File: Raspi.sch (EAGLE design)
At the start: 12 parts

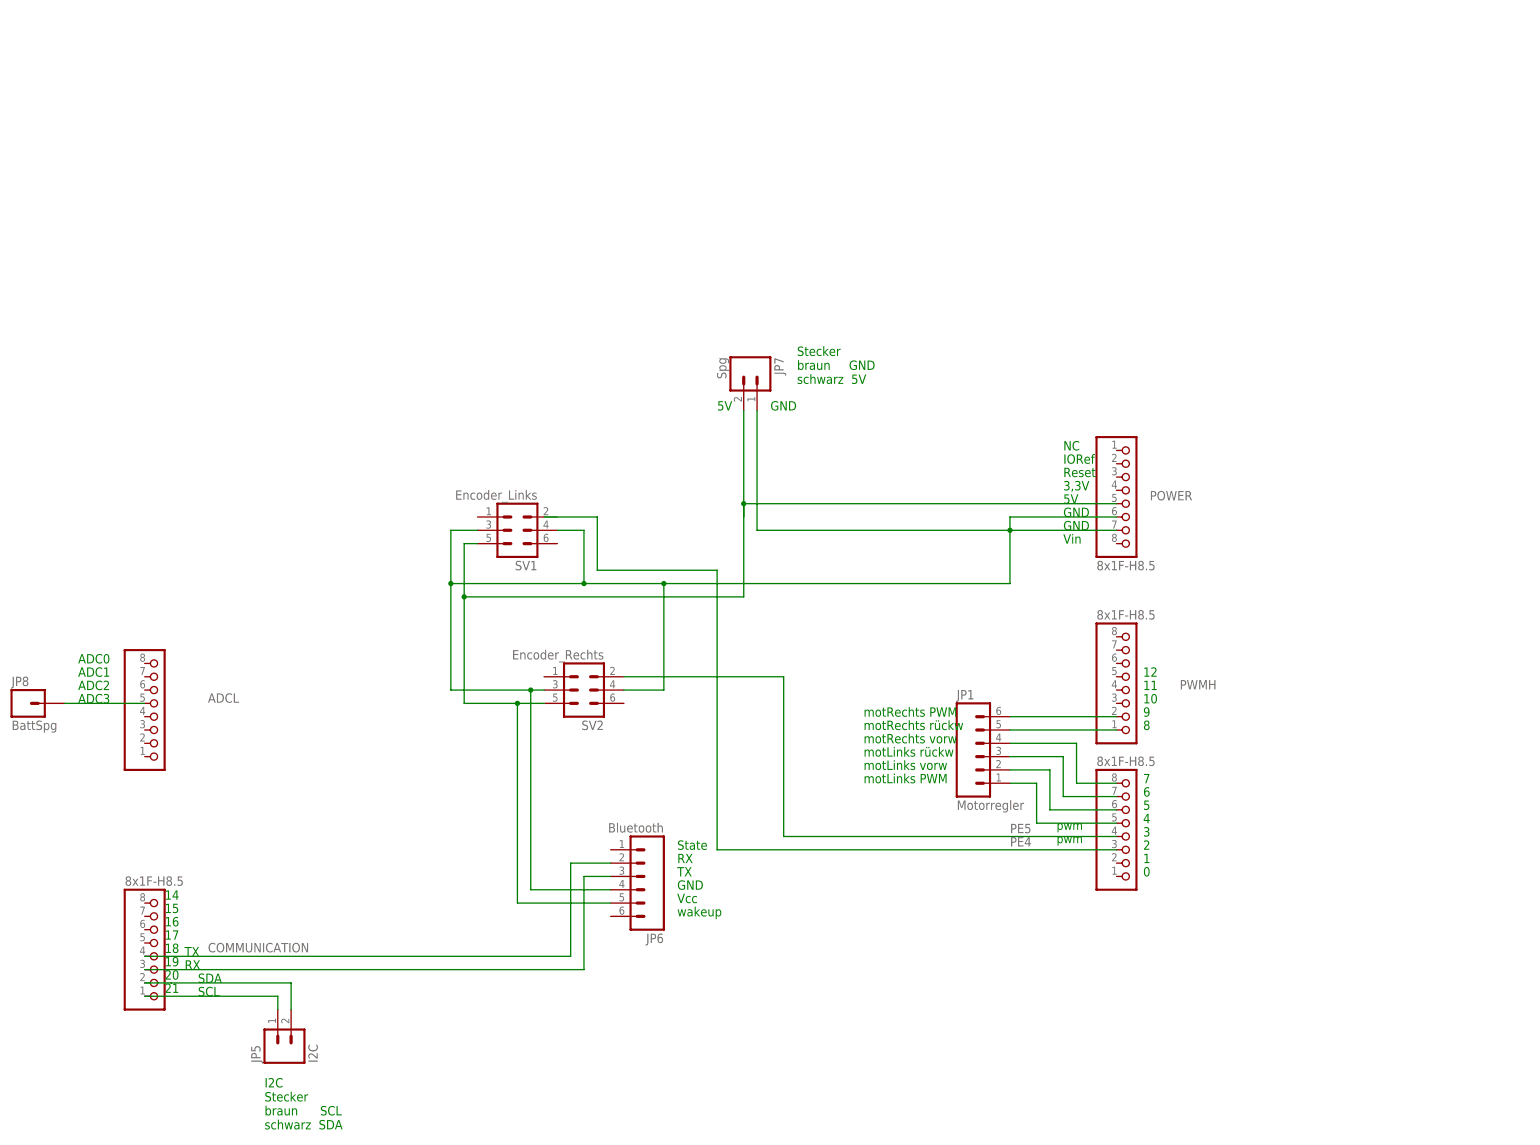
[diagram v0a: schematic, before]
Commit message: 
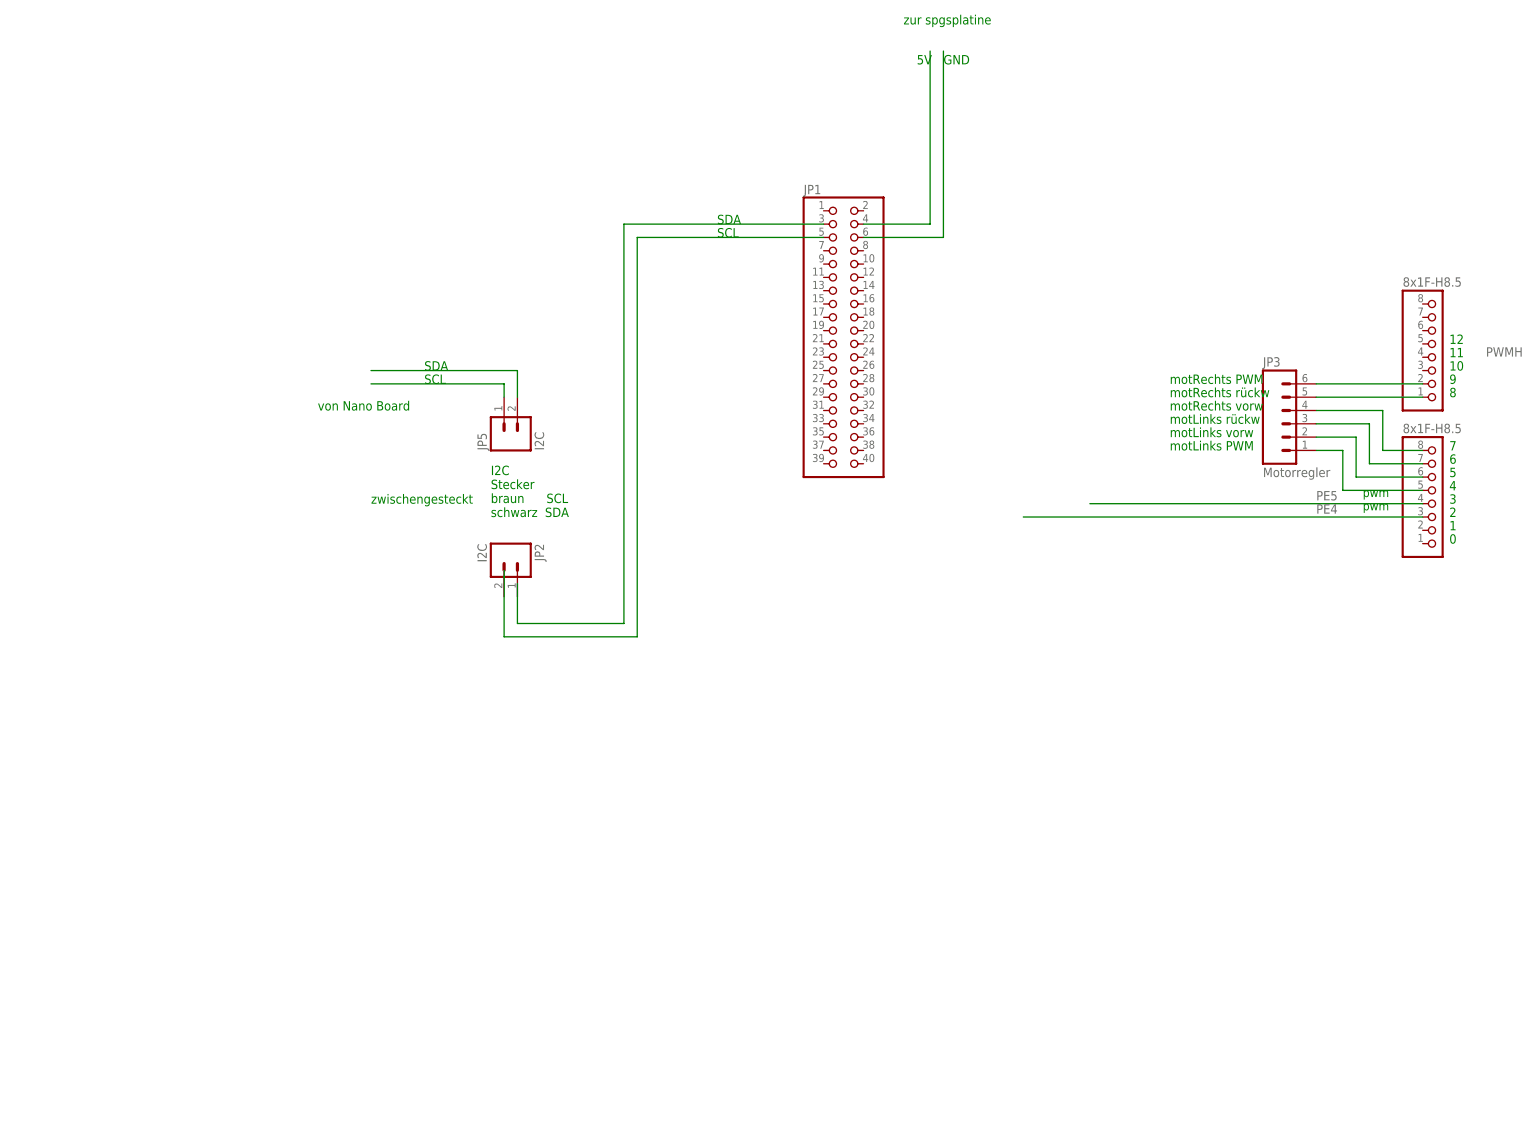
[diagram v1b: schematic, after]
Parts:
- removed ADCL, COMMUNICATION, POWER: 8x1F-H8.5, SmartPrj:PINHD-1X8
- removed JP6: Bluetooth, SparkFun-Connectors:M06LOCK
- removed JP7: Spg, SparkFun-Connectors:M02-JST-2MM-SMT
- removed JP8: BattSpg, SparkFun-Connectors:M01PTH
- removed SV1: Encoder_Links, con-ml:ML6
- removed SV2: Encoder_Rechts, con-ml:ML6
- added JP2: I2C, SparkFun-Connectors:M02-JST-2MM-SMT
- added JP3: Motorregler, SparkFun-Connectors:M06LOCK
- JP1: value Motorregler -> (none); device SparkFun-Connectors:M06LOCK -> adafruit:PINHD-2X20
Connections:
- removed net N$12: COMMUNICATION.3, JP6.3
- removed net N$13: COMMUNICATION.4, JP6.2
- new net N$6: JP3.5, PWMH.1
- net N$1: now also JP1.3; no longer JP6.5, JP7.1, POWER.5, SV1.5, SV2.5
- net N$10: no longer COMMUNICATION.1
- net N$11: no longer COMMUNICATION.2
- net N$16: now also JP3.4; no longer JP1.4
- net N$17: now also JP3.3; no longer JP1.3
- net N$18: now also JP3.2; no longer JP1.2
- net N$19: now also JP3.1; no longer JP1.1
- net N$2: now also JP1.5; no longer JP6.4, JP7.2, POWER.6, POWER.7, SV1.3, SV1.4, SV2.3, SV2.4
- net N$3: now also JP1.4; no longer JP1.6, PWMH.2
- net N$4: now also JP1.6; no longer JP1.5, PWMH.1
- net N$5: now also JP3.6, PWMH.2; no longer ADCL.5, JP8.1
- net PE5: no longer SV2.2
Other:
- note added: "von Nano Board"
- note added: "zur spgsplatine"
- note added: "zwischengesteckt"
- note removed: "14"
- note removed: "15"
- note removed: "16"
- note removed: "17"
- note removed: "18"
- note removed: "19"
- note removed: "20"
- note removed: "21"
- note removed: "3,3V"
- note removed: "ADC0"
- note removed: "ADC1"
- note removed: "ADC2"
- note removed: "ADC3"
- note removed: "IORef"
- note removed: "NC"
- note removed: "RX"
- note removed: "Reset"
- note removed: "State"
- note removed: "Stecker braun GND schwarz 5V"
- note removed: "TX"
- note removed: "Vcc"
- note removed: "Vin"
- note removed: "wakeup"
- moved on the sheet: JP5, PWMH

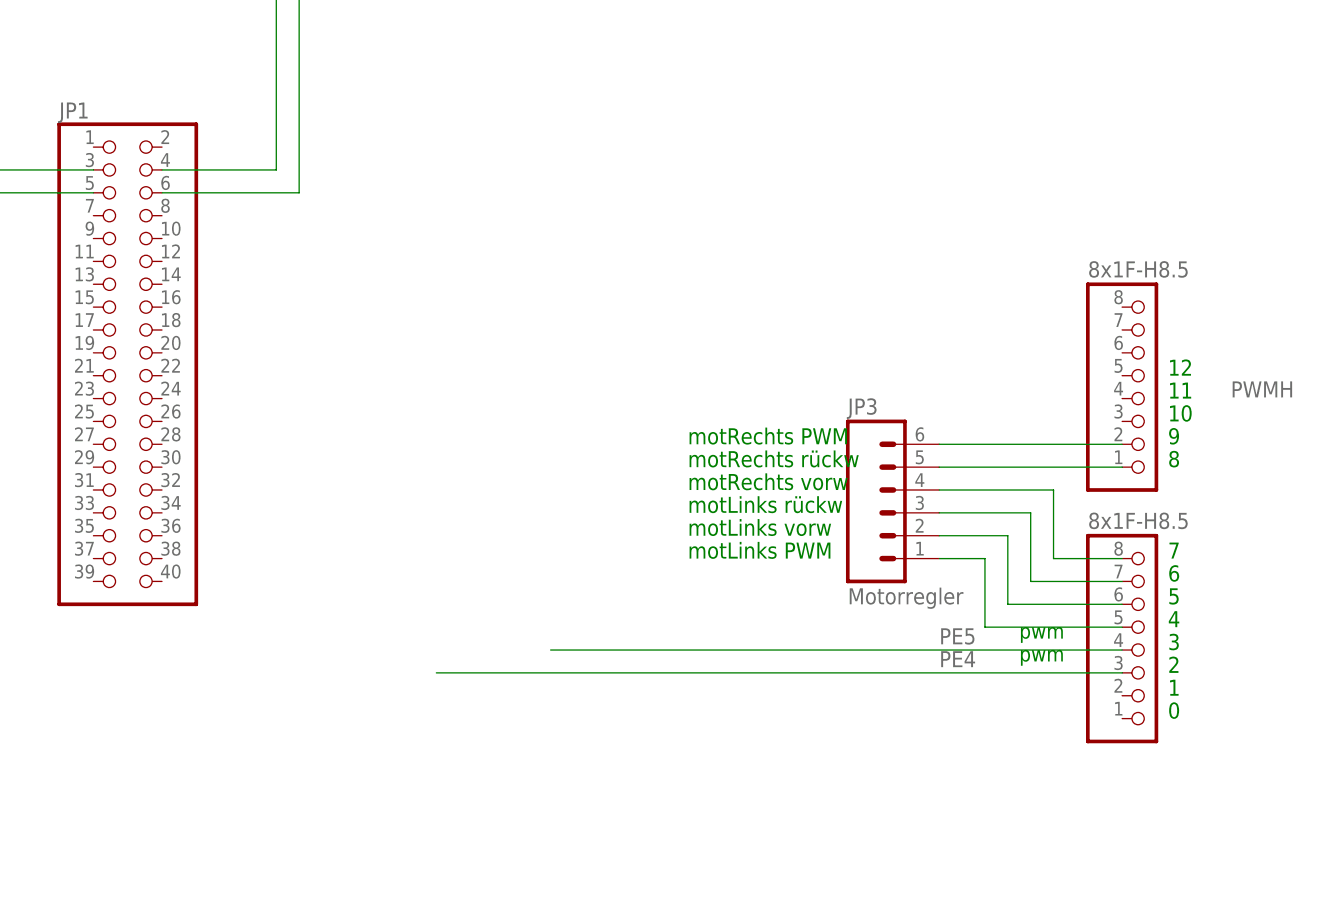
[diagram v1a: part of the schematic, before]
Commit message: 
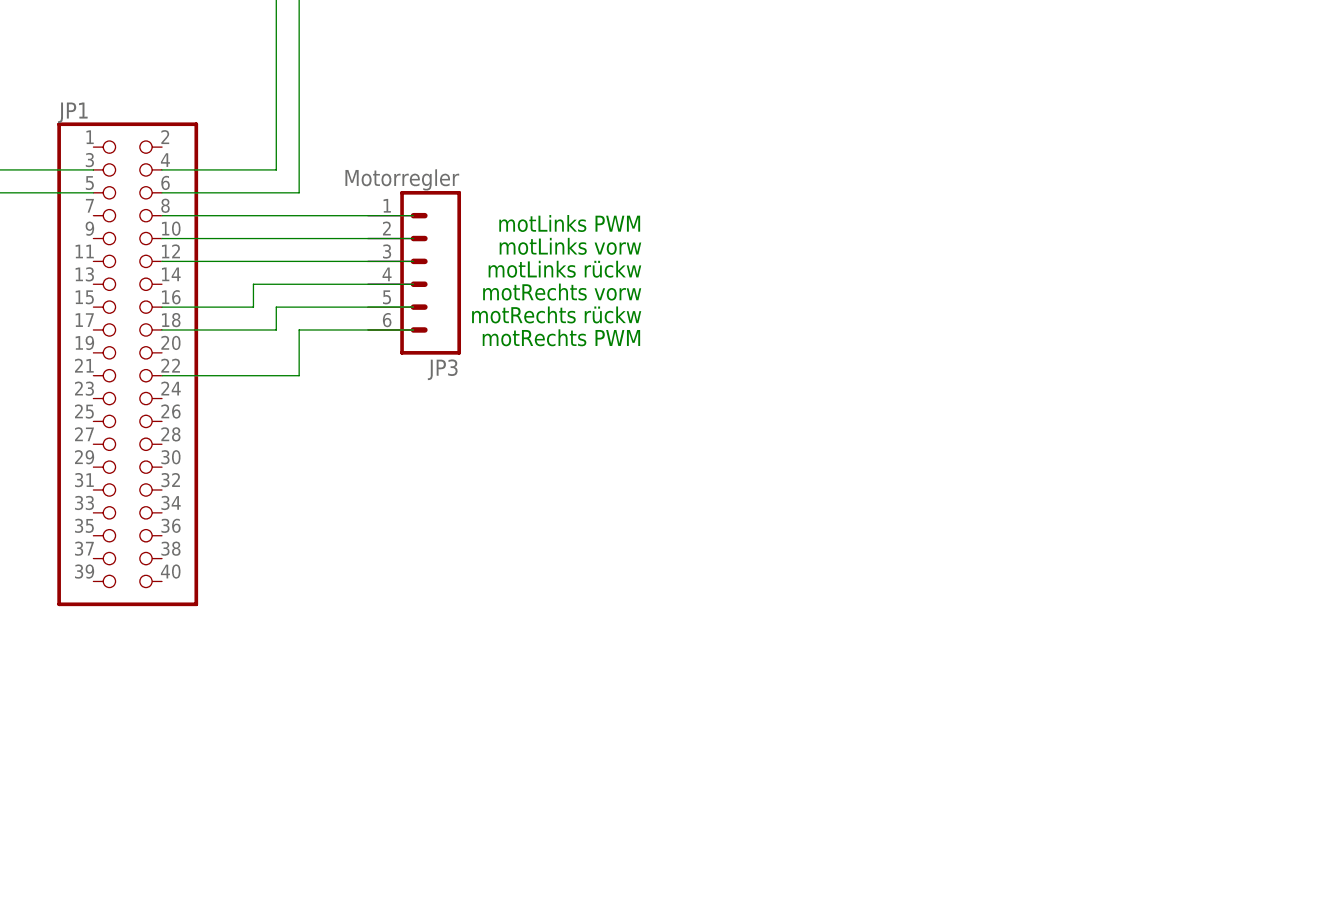
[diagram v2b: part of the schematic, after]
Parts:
- removed PWMH, PWML: 8x1F-H8.5, SmartPrj:PINHD-1X8
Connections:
- removed net N$16: JP3.4, PWML.8
- removed net N$17: JP3.3, PWML.7
- removed net N$18: JP3.2, PWML.6
- removed net N$19: JP3.1, PWML.5
- removed net PE4: PWML.3
- removed net PE5: PWML.4
- new net N$12: JP1.22
- new net N$7: JP1.12
- new net N$8: JP1.16
- new net N$9: JP1.18
- net N$5: now also JP1.8; no longer JP3.6, PWMH.2
- net N$6: now also JP1.10; no longer JP3.5, PWMH.1
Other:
- note removed: "0"
- note removed: "1"
- note removed: "10"
- note removed: "11"
- note removed: "12"
- note removed: "2"
- note removed: "3"
- note removed: "4"
- note removed: "5"
- note removed: "6"
- note removed: "7"
- note removed: "8"
- note removed: "9"
- note removed: "pwm"
- moved on the sheet: JP3
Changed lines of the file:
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@@
 <part name="JP5" library="SparkFun-Connectors" deviceset="M02" device="-JST-2MM-SMT" value="I2C"/>
 <part name="JP2" library="SparkFun-Connectors" deviceset="M02" device="-JST-2MM-SMT" value="I2C"/>
-<part name="PWML" library="SmartPrj" deviceset="PINHD-1X8" device="" value="8x1F-H8.5"/>
-<part name="PWMH" library="SmartPrj" deviceset="PINHD-1X8" device="" value="8x1F-H8.5"/>
 <part name="JP3" library="SparkFun-Connectors" deviceset="M06" device="LOCK" value="Motorregler"/>
 </parts>
@@
 <text x="96.52" y="205.74" size="1.778" layer="91">GND</text>
 <text x="88.9" y="213.36" size="1.778" layer="91">zur spgsplatine</text>
-<text x="193.04" y="114.3" size="1.778" layer="91">0</text>
-<text x="193.04" y="116.84" size="1.778" layer="91">1</text>
-<text x="193.04" y="119.38" size="1.778" layer="91">2</text>
-<text x="193.04" y="121.92" size="1.778" layer="91">3</text>
-<text x="193.04" y="124.46" size="1.778" layer="91">4</text>
-<text x="193.04" y="127" size="1.778" layer="91">5</text>
-<text x="193.04" y="129.54" size="1.778" layer="91">6</text>
-<text x="193.04" y="132.08" size="1.778" layer="91">7</text>
-<text x="176.53" y="120.65" size="1.6764" layer="91">pwm</text>
-<text x="176.53" y="123.19" size="1.6764" layer="91">pwm</text>
-<text x="193.04" y="142.24" size="1.778" layer="91">8</text>
-<text x="193.04" y="144.78" size="1.778" layer="91">9</text>
-<text x="193.04" y="147.32" size="1.778" layer="91">10</text>
-<text x="193.04" y="149.86" size="1.778" layer="91">11</text>
-<text x="193.04" y="152.4" size="1.778" layer="91">12</text>
-<text x="139.7" y="132.08" size="1.778" layer="91">motLinks PWM</text>
-<text x="139.7" y="134.62" size="1.778" layer="91">motLinks vorw</text>
-<text x="139.7" y="137.16" size="1.778" layer="91">motLinks rückw</text>
-<text x="139.7" y="139.7" size="1.778" layer="91">motRechts vorw</text>
-<text x="139.7" y="142.24" size="1.778" layer="91">motRechts rückw</text>
-<text x="139.7" y="144.78" size="1.778" layer="91">motRechts PWM</text>
+<text x="134.62" y="170.18" size="1.778" layer="91" rot="R180">motLinks PWM</text>
+<text x="134.62" y="167.64" size="1.778" layer="91" rot="R180">motLinks vorw</text>
+<text x="134.62" y="165.1" size="1.778" layer="91" rot="R180">motLinks rückw</text>
+<text x="134.62" y="162.56" size="1.778" layer="91" rot="R180">motRechts vorw</text>
+<text x="134.62" y="160.02" size="1.778" layer="91" rot="R180">motRechts rückw</text>
+<text x="134.62" y="157.48" size="1.778" layer="91" rot="R180">motRechts PWM</text>
 </plain>
 <instances>
@@
 <instance part="JP5" gate="G$1" x="15.24" y="134.62" rot="R90"/>
 <instance part="JP2" gate="G$1" x="12.7" y="111.76" rot="R270"/>
-<instance part="PWML" gate="A" x="190.5" y="124.46" smashed="yes" rot="MR180">
-<attribute name="VALUE" x="184.15" y="137.16" size="1.778" layer="96" rot="MR180"/>
-</instance>
-<instance part="PWMH" gate="A" x="190.5" y="152.4" smashed="yes" rot="MR180">
-<attribute name="NAME" x="200.025" y="151.765" size="1.778" layer="95" rot="MR180"/>
-<attribute name="VALUE" x="184.15" y="165.1" size="1.778" layer="96" rot="MR180"/>
-</instance>
-<instance part="JP3" gate="G$1" x="162.56" y="137.16"/>
+<instance part="JP3" gate="G$1" x="109.22" y="165.1" rot="R180"/>
 </instances>
 <busses>
@@
 </segment>
 </net>
-<net name="PE5" class="0">
-<segment>
-<wire x1="124.46" y1="121.92" x2="187.96" y2="121.92" width="0.1524" layer="91"/>
-<label x="167.64" y="122.555" size="1.778" layer="95"/>
-<pinref part="PWML" gate="A" pin="4"/>
-</segment>
-</net>
-<net name="PE4" class="0">
-<segment>
-<wire x1="111.76" y1="119.38" x2="187.96" y2="119.38" width="0.1524" layer="91"/>
-<label x="167.64" y="120.015" size="1.778" layer="95"/>
-<pinref part="PWML" gate="A" pin="3"/>
-</segment>
-</net>
-<net name="N$16" class="0">
-<segment>
-<pinref part="PWML" gate="A" pin="8"/>
-<wire x1="187.96" y1="132.08" x2="180.34" y2="132.08" width="0.1524" layer="91"/>
-<wire x1="180.34" y1="132.08" x2="180.34" y2="139.7" width="0.1524" layer="91"/>
-<pinref part="JP3" gate="G$1" pin="4"/>
-<wire x1="180.34" y1="139.7" x2="167.64" y2="139.7" width="0.1524" layer="91"/>
-</segment>
-</net>
-<net name="N$17" class="0">
-<segment>
-<pinref part="PWML" gate="A" pin="7"/>
-<wire x1="187.96" y1="129.54" x2="177.8" y2="129.54" width="0.1524" layer="91"/>
-<wire x1="177.8" y1="129.54" x2="177.8" y2="137.16" width="0.1524" layer="91"/>
-<pinref part="JP3" gate="G$1" pin="3"/>
-<wire x1="177.8" y1="137.16" x2="167.64" y2="137.16" width="0.1524" layer="91"/>
-</segment>
-</net>
-<net name="N$18" class="0">
-<segment>
-<pinref part="PWML" gate="A" pin="6"/>
-<wire x1="187.96" y1="127" x2="175.26" y2="127" width="0.1524" layer="91"/>
-<wire x1="175.26" y1="127" x2="175.26" y2="134.62" width="0.1524" layer="91"/>
-<pinref part="JP3" gate="G$1" pin="2"/>
-<wire x1="167.64" y1="134.62" x2="175.26" y2="134.62" width="0.1524" layer="91"/>
-</segment>
-</net>
-<net name="N$19" class="0">
-<segment>
-<pinref part="PWML" gate="A" pin="5"/>
-<wire x1="187.96" y1="124.46" x2="172.72" y2="124.46" width="0.1524" layer="91"/>
-<wire x1="172.72" y1="124.46" x2="172.72" y2="132.08" width="0.1524" layer="91"/>
-<pinref part="JP3" gate="G$1" pin="1"/>
-<wire x1="167.64" y1="132.08" x2="172.72" y2="132.08" width="0.1524" layer="91"/>
-</segment>
-</net>
 <net name="N$5" class="0">
 <segment>
-<pinref part="JP3" gate="G$1" pin="6"/>
-<pinref part="PWMH" gate="A" pin="2"/>
-<wire x1="167.64" y1="144.78" x2="187.96" y2="144.78" width="0.1524" layer="91"/>
+<pinref part="JP1" gate="A" pin="8"/>
+<wire x1="81.28" y1="170.18" x2="109.22" y2="170.18" width="0.1524" layer="91"/>
 </segment>
 </net>
 <net name="N$6" class="0">
 <segment>
-<pinref part="JP3" gate="G$1" pin="5"/>
-<pinref part="PWMH" gate="A" pin="1"/>
-<wire x1="167.64" y1="142.24" x2="187.96" y2="142.24" width="0.1524" layer="91"/>
+<pinref part="JP1" gate="A" pin="10"/>
+<wire x1="81.28" y1="167.64" x2="109.22" y2="167.64" width="0.1524" layer="91"/>
 </segment>
 </net>
+<net name="N$8" class="0">
+<segment>
+<pinref part="JP1" gate="A" pin="16"/>
+<wire x1="81.28" y1="160.02" x2="91.44" y2="160.02" width="0.1524" layer="91"/>
+<wire x1="91.44" y1="160.02" x2="91.44" y2="162.56" width="0.1524" layer="91"/>
+<wire x1="91.44" y1="162.56" x2="109.22" y2="162.56" width="0.1524" layer="91"/>
+</segment>
+</net>
+<net name="N$9" class="0">
+<segment>
+<pinref part="JP1" gate="A" pin="18"/>
+<wire x1="81.28" y1="157.48" x2="93.98" y2="157.48" width="0.1524" layer="91"/>
+<wire x1="93.98" y1="157.48" x2="93.98" y2="160.02" width="0.1524" layer="91"/>
+<wire x1="93.98" y1="160.02" x2="109.22" y2="160.02" width="0.1524" layer="91"/>
+</segment>
+</net>
+<net name="N$12" class="0">
+<segment>
+<wire x1="96.52" y1="152.4" x2="96.52" y2="157.48" width="0.1524" layer="91"/>
+<wire x1="96.52" y1="157.48" x2="109.22" y2="157.48" width="0.1524" layer="91"/>
+<pinref part="JP1" gate="A" pin="22"/>
+<wire x1="81.28" y1="152.4" x2="96.52" y2="152.4" width="0.1524" layer="91"/>
+</segment>
+</net>
+<net name="N$7" class="0">
+<segment>
+<pinref part="JP1" gate="A" pin="12"/>
+<wire x1="81.28" y1="165.1" x2="109.22" y2="165.1" width="0.1524" layer="91"/>
+</segment>
+</net>
